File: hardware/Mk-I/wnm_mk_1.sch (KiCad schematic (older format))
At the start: 34 parts, among them SW1 SW_PUSH, SW10 SW_PUSH, SW11 SW_PUSH, SW12 SW_PUSH, SW13 SW_PUSH, SW14 SW_PUSH, SW15 SW_PUSH, SW16 SW_PUSH, SW18 SW_PUSH, SW19 SW_PUSH, SW2 SW_PUSH, SW20 SW_PUSH, SW21 SW_PUSH, SW22 SW_PUSH, SW3 SW_PUSH, SW4 SW_PUSH, SW5 SW_PUSH, SW6 SW_PUSH, SW7 SW_PUSH, SW8 SW_PUSH, SW9 SW_PUSH, U6 encoder_and_switch, U7 encoder_and_switch

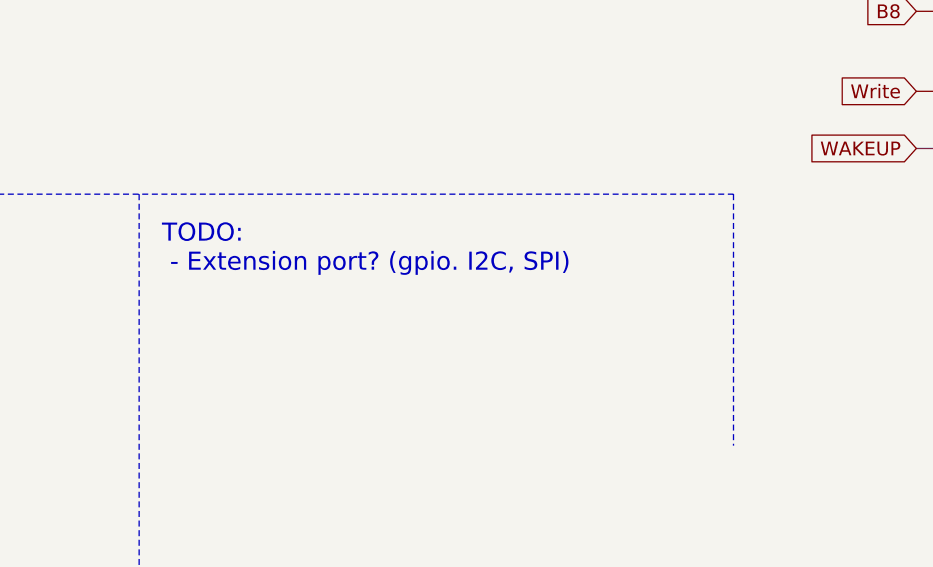
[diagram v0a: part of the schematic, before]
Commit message: HW: Increase board size
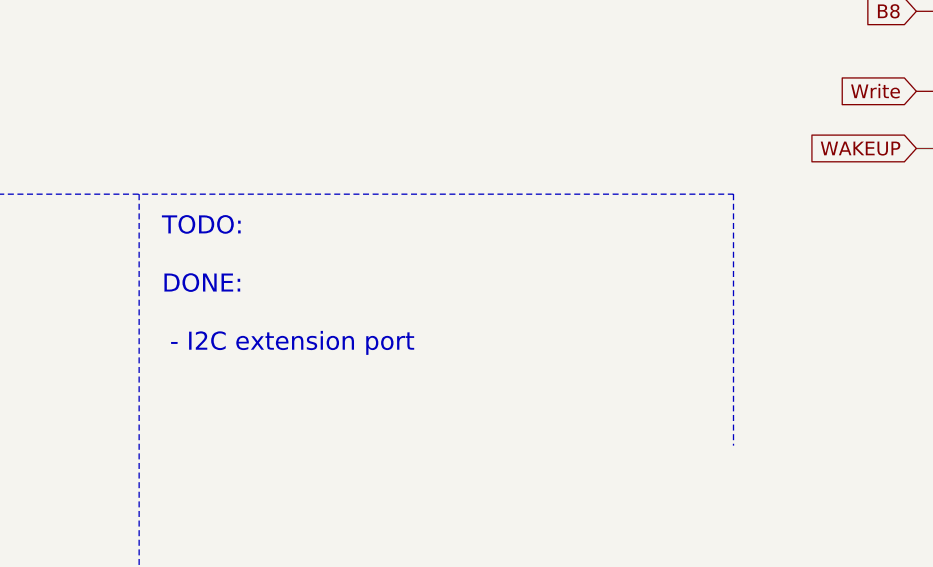
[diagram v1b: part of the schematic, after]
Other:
- note added: "TODO:\n \nDONE:\n\n - I2C extension port"
- note removed: "TODO:\n - Extension port? (gpio. I2C, SPI)"
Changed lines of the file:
@@
 	1    0    0    -1
 $EndComp
-Text Notes 4450 5750 0    79   ~ 0
-TODO:\n - Extension port? (gpio. I2C, SPI)
+Text Notes 4450 6100 0    79   ~ 0
+TODO:\n \nDONE:\n\n - I2C extension port
 Wire Notes Line
 	500  5400 6950 5400

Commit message: HW: Mk-I rev-B
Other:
- note added: "Known problems:\n\nFixed:\n - DAC couplings caps are in series with the chip \n instead of going to GND\n - Voltage regulator footprint\n - Encoders footprints and hole size\n"
- note removed: "Known problems:\n\nFixed:\n - DAC couplings caps are in series with the chip \n instead of going to GND\n - Volatage regulator footprint\n - Encoders footprints and hole size\n"
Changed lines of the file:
@@
 	6950 5400 6950 6500
 Text Notes 600  6400 0    79   ~ 0
-Known problems:\n\nFixed:\n - DAC couplings caps are in series with the chip \n   instead of going to GND\n - Volatage regulator footprint\n - Encoders footprints and hole size\n
+Known problems:\n\nFixed:\n - DAC couplings caps are in series with the chip \n   instead of going to GND\n - Voltage regulator footprint\n - Encoders footprints and hole size\n
 $EndSCHEMATC

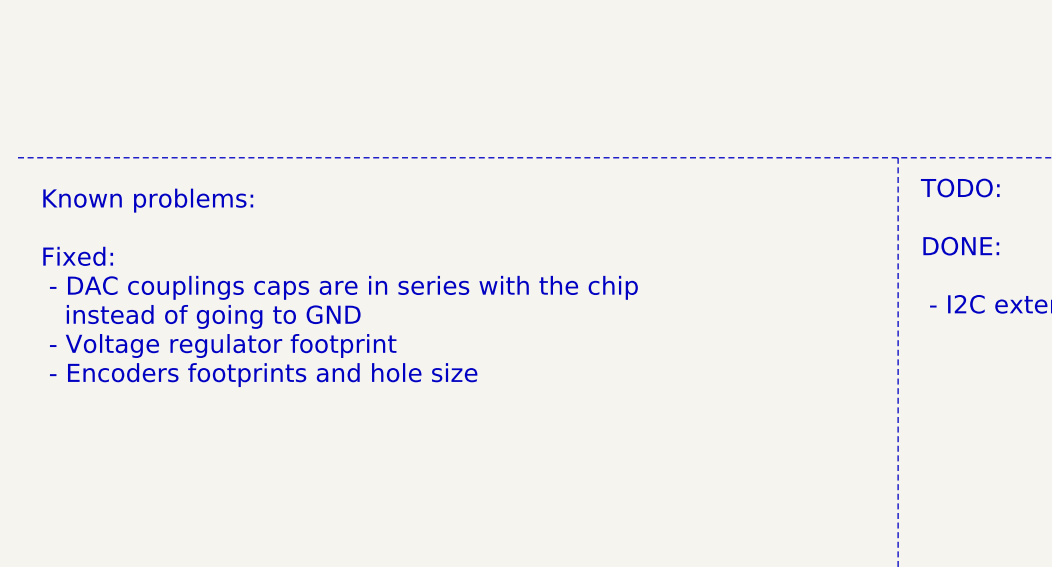
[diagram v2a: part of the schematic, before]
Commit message: HW: Start rev-C with DAC VDDD fix
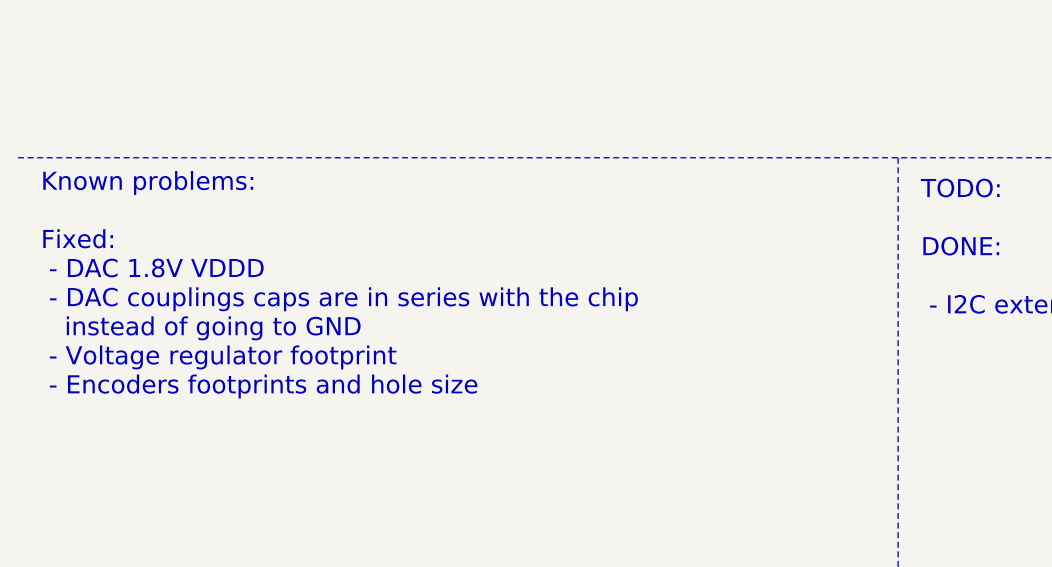
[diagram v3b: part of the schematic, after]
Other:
- note added: "Known problems:\n\nFixed:\n - DAC 1.8V VDDD\n - DAC couplings caps are in series with the chip \n instead of going to GND\n - Voltage regulator footprint\n - Encoders footprints and hole size\n"
- note removed: "Known problems:\n\nFixed:\n - DAC couplings caps are in series with the chip \n instead of going to GND\n - Voltage regulator footprint\n - Encoders footprints and hole size\n"
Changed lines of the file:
@@
 Title "Wee Noise Maker - Mk-I"
 Date ""
-Rev "B"
+Rev "C"
 Comp "Fabien Chouteau"
 Comment1 ""
@@
 Wire Notes Line
 	6950 5400 6950 6500
-Text Notes 600  6400 0    79   ~ 0
-Known problems:\n\nFixed:\n - DAC couplings caps are in series with the chip \n   instead of going to GND\n - Voltage regulator footprint\n - Encoders footprints and hole size\n
+Text Notes 600  6450 0    79   ~ 0
+Known problems:\n\nFixed:\n - DAC 1.8V VDDD\n - DAC couplings caps are in series with the chip \n   instead of going to GND\n - Voltage regulator footprint\n - Encoders footprints and hole size\n
 $EndSCHEMATC

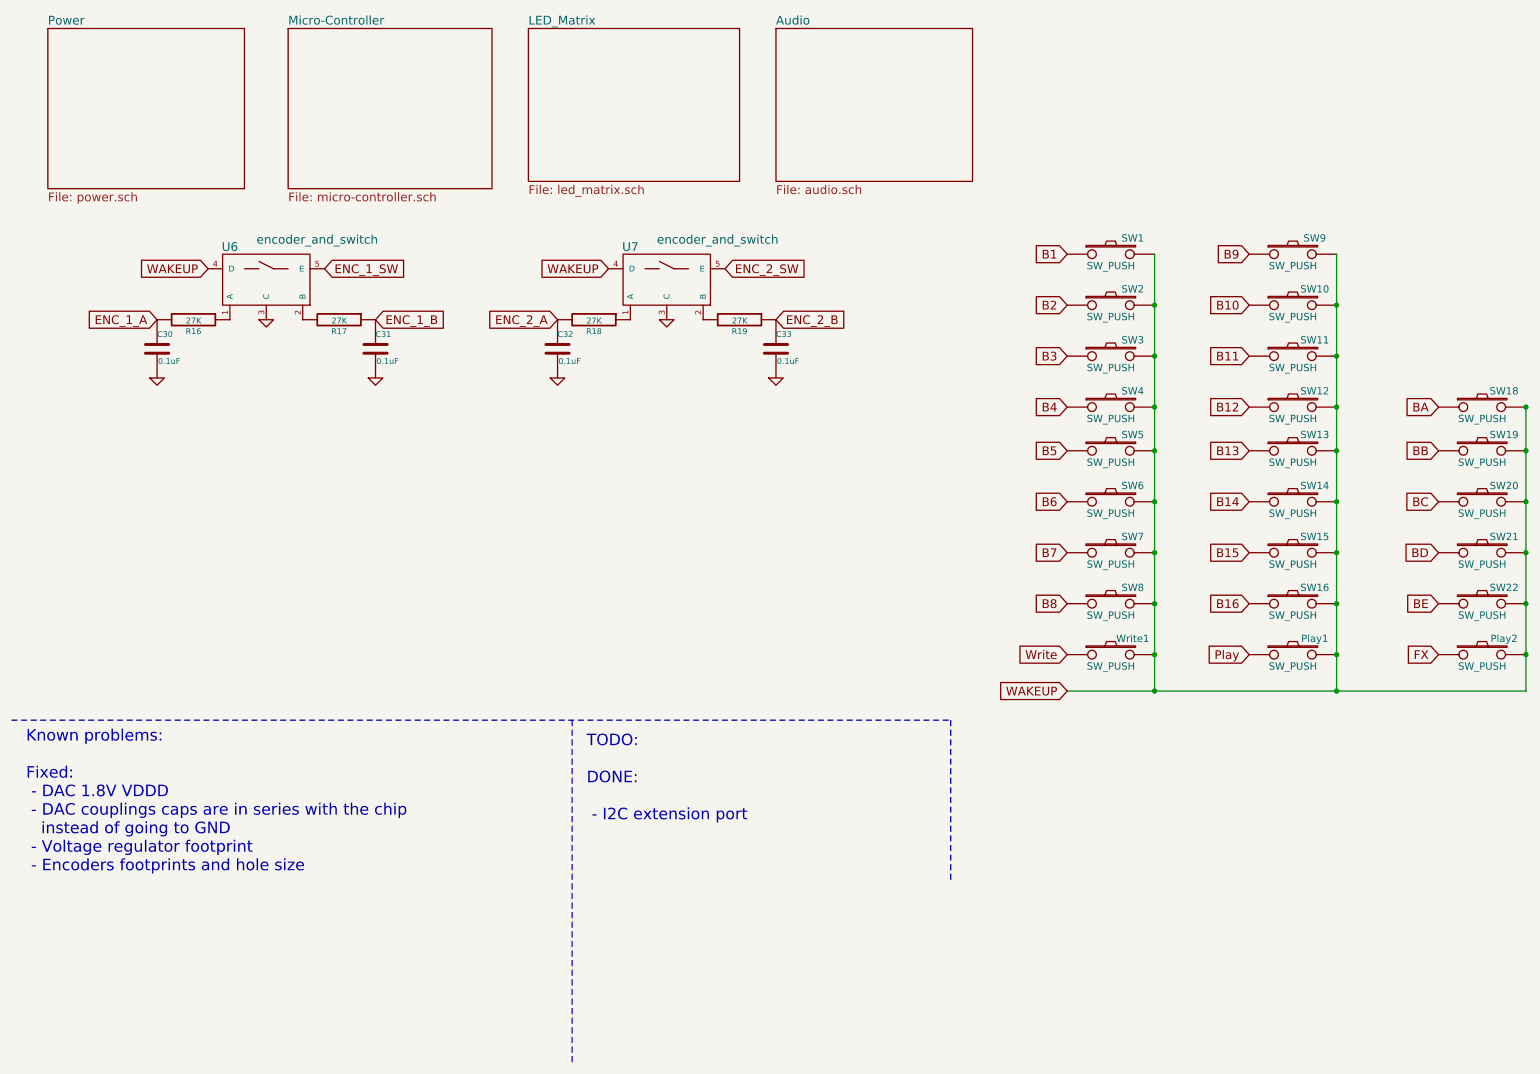
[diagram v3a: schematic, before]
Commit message: HW: Update parts value
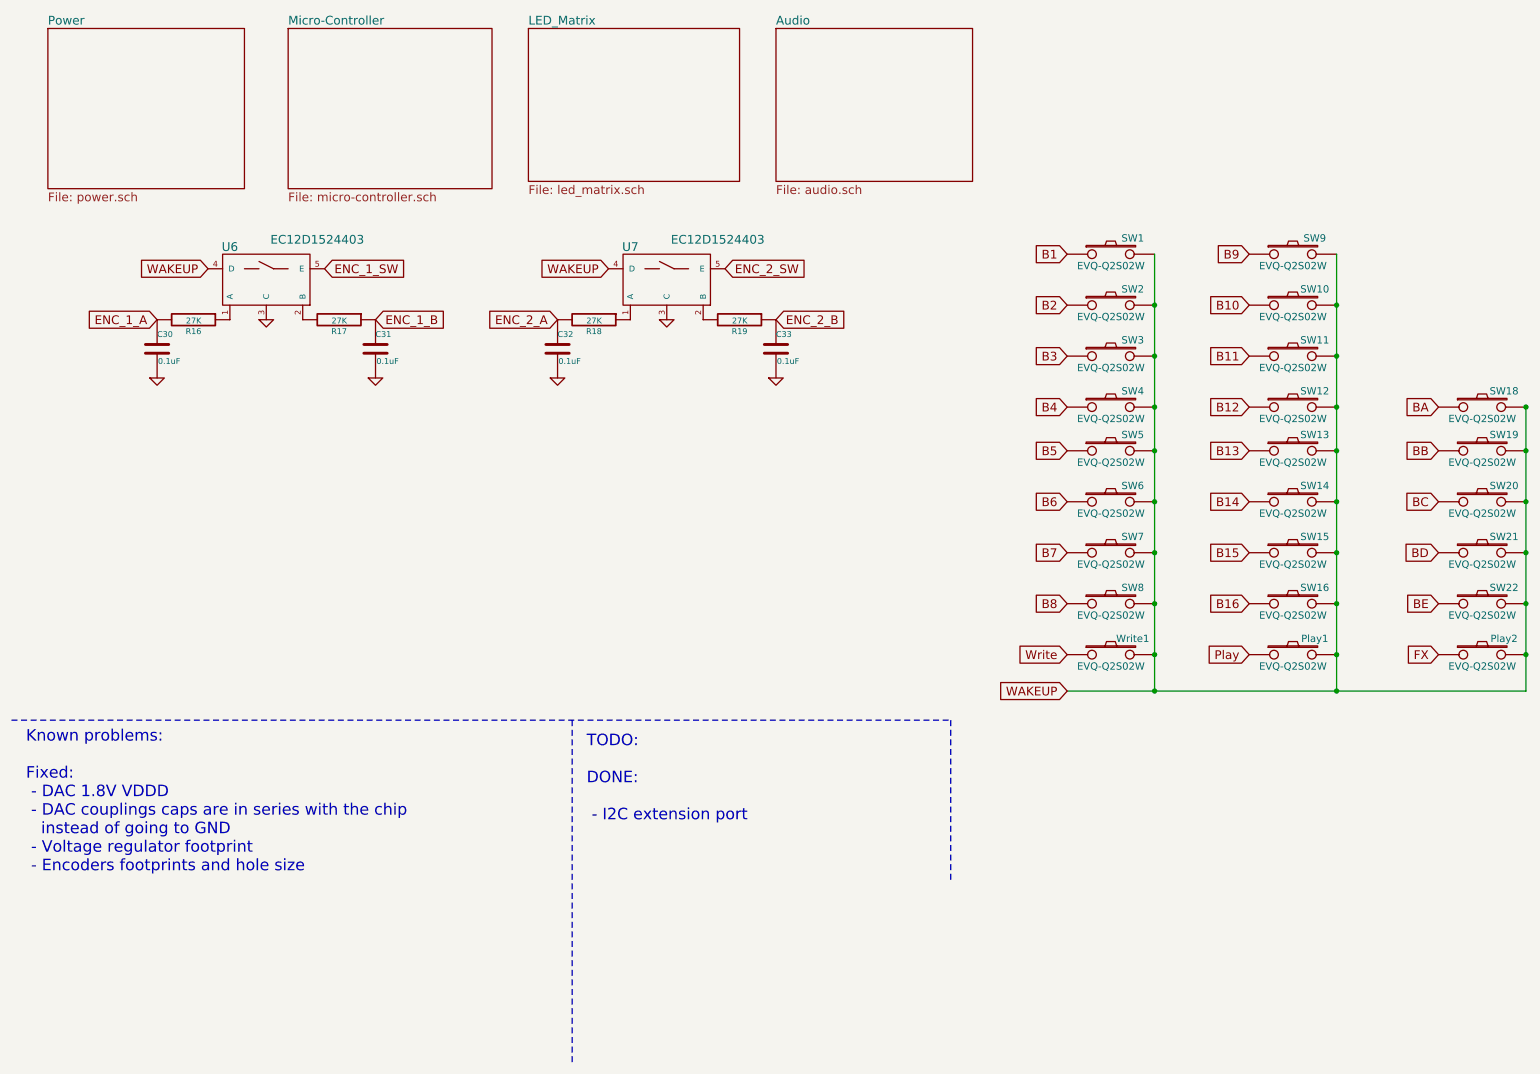
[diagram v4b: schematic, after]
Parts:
- Play1, Play2, SW1, SW10, SW11, SW12, SW13, SW14, SW15, SW16, SW18, SW19, SW2, SW20, SW21, SW22, SW3, SW4, SW5, SW6, SW7, SW8, SW9, Write1: value SW_PUSH -> EVQ-Q2S02W
- U6, U7: value encoder_and_switch -> EC12D1524403
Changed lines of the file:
@@
 P 8050 2200
 F 0 "SW1" H 8200 2310 50  0000 C CNN
-F 1 "SW_PUSH" H 8050 2120 50  0000 C CNN
+F 1 "EVQ-Q2S02W" H 8050 2120 50  0000 C CNN
 F 2 "Buttons_Switches_SMD:SW_SPST_B3SL-1002P" H 8050 2200 50  0001 C CNN
 F 3 "" H 8050 2200 50  0000 C CNN
@@
 P 8050 2550
 F 0 "SW2" H 8200 2660 50  0000 C CNN
-F 1 "SW_PUSH" H 8050 2470 50  0000 C CNN
+F 1 "EVQ-Q2S02W" H 8050 2470 50  0000 C CNN
 F 2 "Buttons_Switches_SMD:SW_SPST_B3SL-1002P" H 8050 2550 50  0001 C CNN
 F 3 "" H 8050 2550 50  0000 C CNN
@@
 P 8050 2900
 F 0 "SW3" H 8200 3010 50  0000 C CNN
-F 1 "SW_PUSH" H 8050 2820 50  0000 C CNN
+F 1 "EVQ-Q2S02W" H 8050 2820 50  0000 C CNN
 F 2 "Buttons_Switches_SMD:SW_SPST_B3SL-1002P" H 8050 2900 50  0001 C CNN
 F 3 "" H 8050 2900 50  0000 C CNN
@@
 P 8050 3250
 F 0 "SW4" H 8200 3360 50  0000 C CNN
-F 1 "SW_PUSH" H 8050 3170 50  0000 C CNN
+F 1 "EVQ-Q2S02W" H 8050 3170 50  0000 C CNN
 F 2 "Buttons_Switches_SMD:SW_SPST_B3SL-1002P" H 8050 3250 50  0001 C CNN
 F 3 "" H 8050 3250 50  0000 C CNN
@@
 P 8050 3550
 F 0 "SW5" H 8200 3660 50  0000 C CNN
-F 1 "SW_PUSH" H 8050 3470 50  0000 C CNN
+F 1 "EVQ-Q2S02W" H 8050 3470 50  0000 C CNN
 F 2 "Buttons_Switches_SMD:SW_SPST_B3SL-1002P" H 8050 3550 50  0001 C CNN
 F 3 "" H 8050 3550 50  0000 C CNN
@@
 P 8050 3900
 F 0 "SW6" H 8200 4010 50  0000 C CNN
-F 1 "SW_PUSH" H 8050 3820 50  0000 C CNN
+F 1 "EVQ-Q2S02W" H 8050 3820 50  0000 C CNN
 F 2 "Buttons_Switches_SMD:SW_SPST_B3SL-1002P" H 8050 3900 50  0001 C CNN
 F 3 "" H 8050 3900 50  0000 C CNN
@@
 P 8050 4250
 F 0 "SW7" H 8200 4360 50  0000 C CNN
-F 1 "SW_PUSH" H 8050 4170 50  0000 C CNN
+F 1 "EVQ-Q2S02W" H 8050 4170 50  0000 C CNN
 F 2 "Buttons_Switches_SMD:SW_SPST_B3SL-1002P" H 8050 4250 50  0001 C CNN
 F 3 "" H 8050 4250 50  0000 C CNN
@@
 P 8050 4600
 F 0 "SW8" H 8200 4710 50  0000 C CNN
-F 1 "SW_PUSH" H 8050 4520 50  0000 C CNN
+F 1 "EVQ-Q2S02W" H 8050 4520 50  0000 C CNN
 F 2 "Buttons_Switches_SMD:SW_SPST_B3SL-1002P" H 8050 4600 50  0001 C CNN
 F 3 "" H 8050 4600 50  0000 C CNN
@@
 P 9300 2200
 F 0 "SW9" H 9450 2310 50  0000 C CNN
-F 1 "SW_PUSH" H 9300 2120 50  0000 C CNN
+F 1 "EVQ-Q2S02W" H 9300 2120 50  0000 C CNN
 F 2 "Buttons_Switches_SMD:SW_SPST_B3SL-1002P" H 9300 2200 50  0001 C CNN
 F 3 "" H 9300 2200 50  0000 C CNN
@@
 P 9300 2550
 F 0 "SW10" H 9450 2660 50  0000 C CNN
-F 1 "SW_PUSH" H 9300 2470 50  0000 C CNN
+F 1 "EVQ-Q2S02W" H 9300 2470 50  0000 C CNN
 F 2 "Buttons_Switches_SMD:SW_SPST_B3SL-1002P" H 9300 2550 50  0001 C CNN
 F 3 "" H 9300 2550 50  0000 C CNN
@@
 P 9300 2900
 F 0 "SW11" H 9450 3010 50  0000 C CNN
-F 1 "SW_PUSH" H 9300 2820 50  0000 C CNN
+F 1 "EVQ-Q2S02W" H 9300 2820 50  0000 C CNN
 F 2 "Buttons_Switches_SMD:SW_SPST_B3SL-1002P" H 9300 2900 50  0001 C CNN
 F 3 "" H 9300 2900 50  0000 C CNN
@@
 P 9300 3250
 F 0 "SW12" H 9450 3360 50  0000 C CNN
-F 1 "SW_PUSH" H 9300 3170 50  0000 C CNN
+F 1 "EVQ-Q2S02W" H 9300 3170 50  0000 C CNN
 F 2 "Buttons_Switches_SMD:SW_SPST_B3SL-1002P" H 9300 3250 50  0001 C CNN
 F 3 "" H 9300 3250 50  0000 C CNN
@@
 P 9300 3550
 F 0 "SW13" H 9450 3660 50  0000 C CNN
-F 1 "SW_PUSH" H 9300 3470 50  0000 C CNN
+F 1 "EVQ-Q2S02W" H 9300 3470 50  0000 C CNN
 F 2 "Buttons_Switches_SMD:SW_SPST_B3SL-1002P" H 9300 3550 50  0001 C CNN
 F 3 "" H 9300 3550 50  0000 C CNN
@@
 P 9300 3900
 F 0 "SW14" H 9450 4010 50  0000 C CNN
-F 1 "SW_PUSH" H 9300 3820 50  0000 C CNN
+F 1 "EVQ-Q2S02W" H 9300 3820 50  0000 C CNN
 F 2 "Buttons_Switches_SMD:SW_SPST_B3SL-1002P" H 9300 3900 50  0001 C CNN
 F 3 "" H 9300 3900 50  0000 C CNN
@@
 P 9300 4250
 F 0 "SW15" H 9450 4360 50  0000 C CNN
-F 1 "SW_PUSH" H 9300 4170 50  0000 C CNN
+F 1 "EVQ-Q2S02W" H 9300 4170 50  0000 C CNN
 F 2 "Buttons_Switches_SMD:SW_SPST_B3SL-1002P" H 9300 4250 50  0001 C CNN
 F 3 "" H 9300 4250 50  0000 C CNN
@@
 P 9300 4600
 F 0 "SW16" H 9450 4710 50  0000 C CNN
-F 1 "SW_PUSH" H 9300 4520 50  0000 C CNN
+F 1 "EVQ-Q2S02W" H 9300 4520 50  0000 C CNN
 F 2 "Buttons_Switches_SMD:SW_SPST_B3SL-1002P" H 9300 4600 50  0001 C CNN
 F 3 "" H 9300 4600 50  0000 C CNN
@@
 P 8050 4950
 F 0 "Write1" H 8200 5060 50  0000 C CNN
-F 1 "SW_PUSH" H 8050 4870 50  0000 C CNN
+F 1 "EVQ-Q2S02W" H 8050 4870 50  0000 C CNN
 F 2 "Buttons_Switches_SMD:SW_SPST_B3SL-1002P" H 8050 4950 50  0001 C CNN
 F 3 "" H 8050 4950 50  0000 C CNN
@@
 P 9300 4950
 F 0 "Play1" H 9450 5060 50  0000 C CNN
-F 1 "SW_PUSH" H 9300 4870 50  0000 C CNN
+F 1 "EVQ-Q2S02W" H 9300 4870 50  0000 C CNN
 F 2 "Buttons_Switches_SMD:SW_SPST_B3SL-1002P" H 9300 4950 50  0001 C CNN
 F 3 "" H 9300 4950 50  0000 C CNN
@@
 P 10600 3250
 F 0 "SW18" H 10750 3360 50  0000 C CNN
-F 1 "SW_PUSH" H 10600 3170 50  0000 C CNN
+F 1 "EVQ-Q2S02W" H 10600 3170 50  0000 C CNN
 F 2 "Buttons_Switches_SMD:SW_SPST_B3SL-1002P" H 10600 3250 50  0001 C CNN
 F 3 "" H 10600 3250 50  0000 C CNN
@@
 P 10600 3550
 F 0 "SW19" H 10750 3660 50  0000 C CNN
-F 1 "SW_PUSH" H 10600 3470 50  0000 C CNN
+F 1 "EVQ-Q2S02W" H 10600 3470 50  0000 C CNN
 F 2 "Buttons_Switches_SMD:SW_SPST_B3SL-1002P" H 10600 3550 50  0001 C CNN
 F 3 "" H 10600 3550 50  0000 C CNN
@@
 P 10600 3900
 F 0 "SW20" H 10750 4010 50  0000 C CNN
-F 1 "SW_PUSH" H 10600 3820 50  0000 C CNN
+F 1 "EVQ-Q2S02W" H 10600 3820 50  0000 C CNN
 F 2 "Buttons_Switches_SMD:SW_SPST_B3SL-1002P" H 10600 3900 50  0001 C CNN
 F 3 "" H 10600 3900 50  0000 C CNN
@@
 P 10600 4250
 F 0 "SW21" H 10750 4360 50  0000 C CNN
-F 1 "SW_PUSH" H 10600 4170 50  0000 C CNN
+F 1 "EVQ-Q2S02W" H 10600 4170 50  0000 C CNN
 F 2 "Buttons_Switches_SMD:SW_SPST_B3SL-1002P" H 10600 4250 50  0001 C CNN
 F 3 "" H 10600 4250 50  0000 C CNN
@@
 P 10600 4600
 F 0 "SW22" H 10750 4710 50  0000 C CNN
-F 1 "SW_PUSH" H 10600 4520 50  0000 C CNN
+F 1 "EVQ-Q2S02W" H 10600 4520 50  0000 C CNN
 F 2 "Buttons_Switches_SMD:SW_SPST_B3SL-1002P" H 10600 4600 50  0001 C CNN
 F 3 "" H 10600 4600 50  0000 C CNN
@@
 P 10600 4950
 F 0 "Play2" H 10750 5060 50  0000 C CNN
-F 1 "SW_PUSH" H 10600 4870 50  0000 C CNN
+F 1 "EVQ-Q2S02W" H 10600 4870 50  0000 C CNN
 F 2 "Buttons_Switches_SMD:SW_SPST_B3SL-1002P" H 10600 4950 50  0001 C CNN
 F 3 "" H 10600 4950 50  0000 C CNN
@@
 P 2250 1950
 F 0 "U6" H 2000 1750 60  0000 C CNN
-F 1 "encoder_and_switch" H 2600 1800 60  0000 C CNN
+F 1 "EC12D1524403" H 2600 1800 60  0000 C CNN
 F 2 "POSS:encoder_EC12D" H 2250 1950 60  0001 C CNN
 F 3 "" H 2250 1950 60  0001 C CNN
@@
 P 5000 1950
 F 0 "U7" H 4750 1750 60  0000 C CNN
-F 1 "encoder_and_switch" H 5350 1800 60  0000 C CNN
+F 1 "EC12D1524403" H 5350 1800 60  0000 C CNN
 F 2 "POSS:encoder_EC12D" H 5000 1950 60  0001 C CNN
 F 3 "" H 5000 1950 60  0001 C CNN
